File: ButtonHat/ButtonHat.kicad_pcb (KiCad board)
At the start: 2 copper layers, 65 x 56 mm, 40 parts, among them J0 RPI_GPIO, J1 1 2 3 4 5 6, J2 7 8 9 10 11 12, J3 4 17 27 22 5 6, J4 18 23 24 25 12 16, T1 1 2 3 4 5 6, T2 Ground, T3 7 8 9 10 11 12, U1 74AHC14, U2 74AHC14

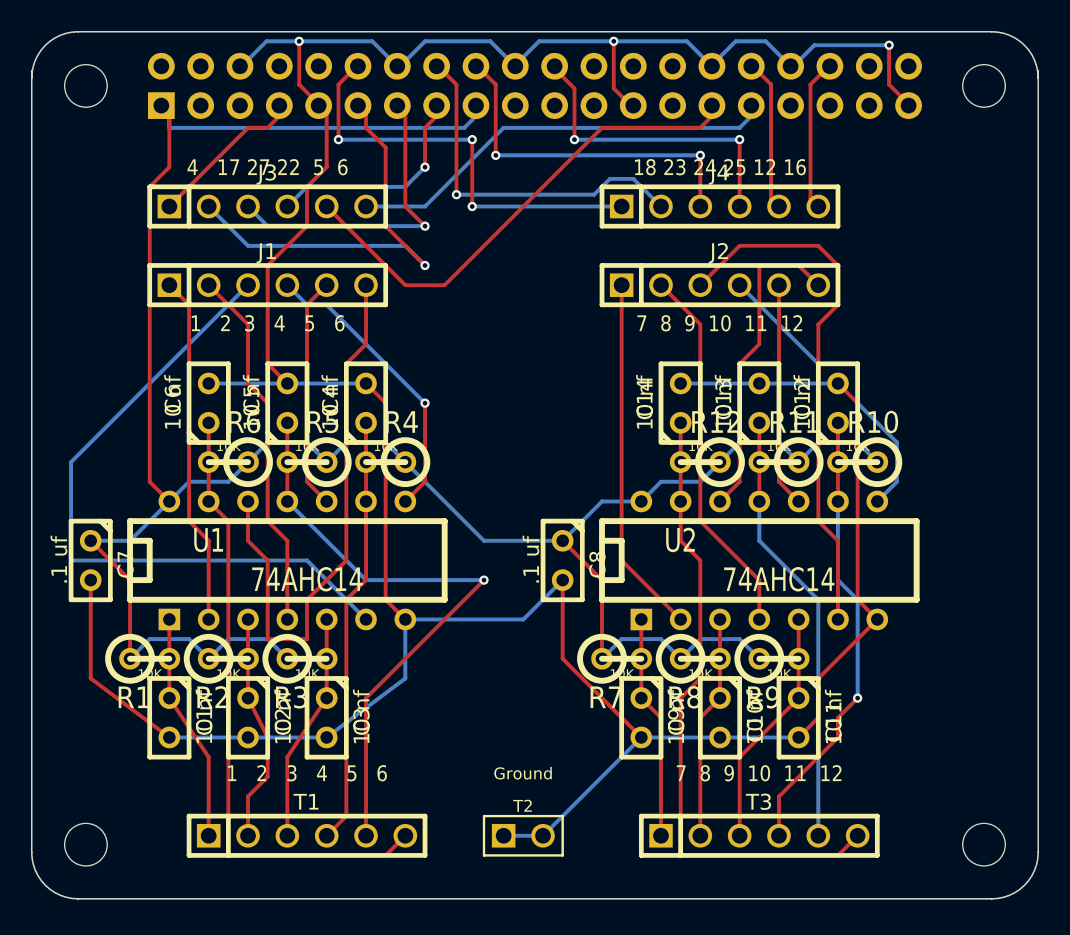
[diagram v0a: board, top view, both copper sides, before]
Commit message: Update GPIO Hats: make all 17 GPIO pins available on a socket header strip.
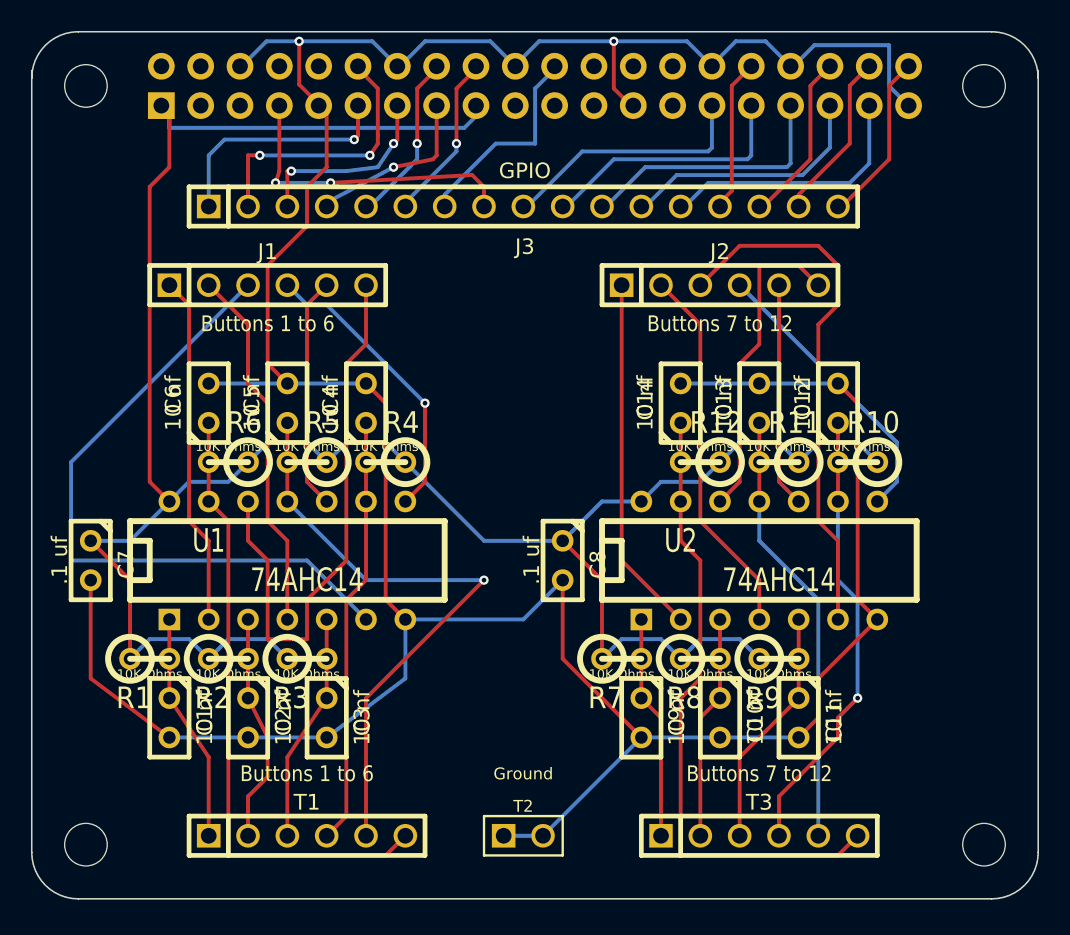
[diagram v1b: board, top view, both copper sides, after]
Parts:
- removed J4: 18 23 24 25 12 16, PIN_ARRAY-6X1
- J1: value 1 2 3 4 5 6 -> Buttons 1 to 6; footprint PIN_ARRAY-6X1 -> PIN_HEADER-6X1
- J2, T3: value 7 8 9 10 11 12 -> Buttons 7 to 12
- J3: value 4 17 27 22 5 6 -> GPIO; footprint PIN_ARRAY-6X1 -> PIN_HEADER_17x1
- R1, R10, R11, R12, R2, R3, R4, R5, R6, R7, R8, R9: value 10K -> 10K Ohms
- T1: value 1 2 3 4 5 6 -> Buttons 1 to 6
- moved J3 16.5 mm to (69.8, 43.2)
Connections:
- net N-0000013 renamed BCM22, wPi 3
- net N-0000014 renamed BCM27, wPi 2
- J0 pad 11: N-0000015 -> BCM17, wPi 0
- J0 pad 12: N-0000010 (its old number) -> BCM18, wPi 1
- J0 pad 16: N-0000022 -> BCM23, wPi 4
- J0 pad 18: N-000009 (its old number) -> BCM24, wPi 5
- J0 pad 22: N-000008 (its old number) -> BCM25, wPi 6
- J0 pad 29: N-0000012 -> BCM5, wPi 21
- J0 pad 31: N-0000011 -> BCM6, wPi 22
- J0 pad 32: N-000007 (its old number) -> BCM12, wPi 26
- J0 pad 33: (no net) -> BCM13, wPi 23
- J0 pad 35: (no net) -> BCM19, wPi 24
- J0 pad 36: N-0000024 -> BCM16, wPi 27
- J0 pad 37: (no net) -> BCM26, wPi 25
- J0 pad 38: (no net) -> BCM20, wPi 28
- J0 pad 40: (no net) -> BCM21, wPi 29
- J0 pad 7: N-0000016 -> BCM4, wPi 7
- J3 pad 1: N-0000016 -> BCM17, wPi 0
- J3 pad 2: N-0000015 -> BCM18, wPi 1
- J3 pad 5: N-0000012 -> BCM23, wPi 4
- J3 pad 6: N-0000011 -> BCM24, wPi 5
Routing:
- net N-0000012: track 32.8 -> 0.00 mm
- net N-0000011: track 28.6 -> 0.00 mm
- net N-0000010 (its old number): track 27.9 -> 0.00 mm, vias 3 -> 0
- net N-0000015: track 27.8 -> 0.00 mm, vias 1 -> 0
- net N-0000022: track 23.2 -> 0.00 mm, vias 1 -> 0
- net N-000009 (its old number): track 22.9 -> 0.00 mm, vias 2 -> 0
- net N-000008 (its old number): track 20.3 -> 0.00 mm, vias 2 -> 0
- net BCM4, wPi 7: track 0.00 -> 20.1 mm, vias 0 -> 2
- net BCM18, wPi 1: track 0.00 -> 17.6 mm, vias 0 -> 2
- net BCM26, wPi 25: track 0.00 -> 17.1 mm
- net BCM13, wPi 23: track 0.00 -> 17.1 mm
- net BCM6, wPi 22: track 0.00 -> 16.8 mm
- net BCM5, wPi 21: track 0.00 -> 16.5 mm
- net BCM19, wPi 24: track 0.00 -> 16.5 mm
- net BCM17, wPi 0: track 0.00 -> 15.4 mm, vias 0 -> 1
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
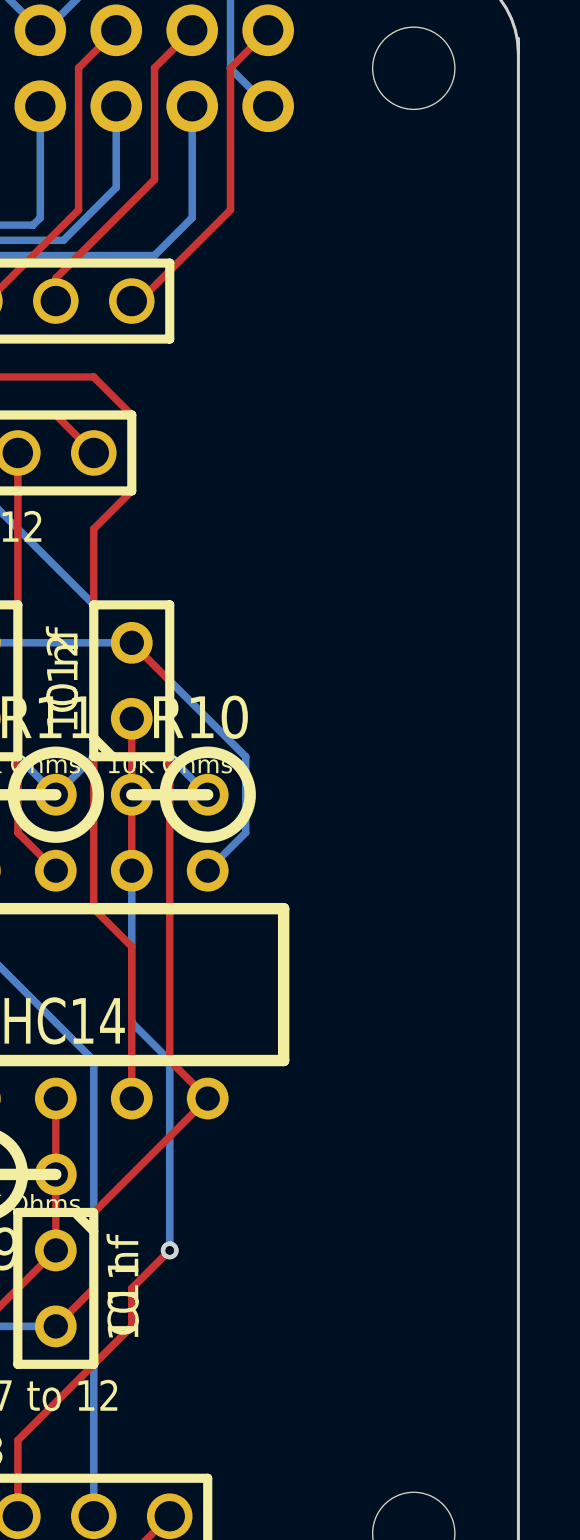
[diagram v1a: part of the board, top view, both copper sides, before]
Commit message: Add copyright notice to ButtonHat and LEDDriverHat.
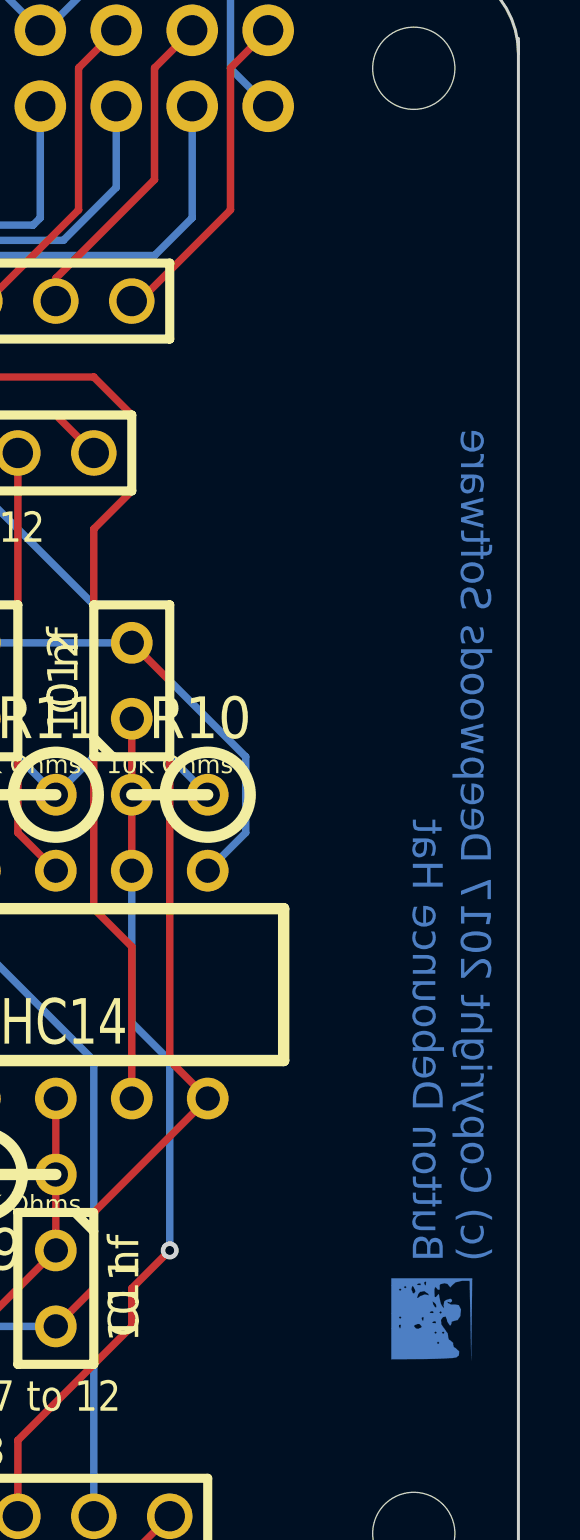
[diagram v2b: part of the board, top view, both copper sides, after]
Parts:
- added ?: , DWSLogoBCU, F.Cu at (100.2, 77.2)
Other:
- board text added: "(c) Copyright 2017 Deepwoods Software Button Debounce Hat"
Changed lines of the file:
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@@
     (area 29.28939 20.694 130.847429 101.769)
     (thickness 1.6)
-    (drawings 16)
+    (drawings 17)
     (tracks 345)
     (zones 0)
-    (modules 39)
+    (modules 40)
     (nets 44)
   )
@@
     )
   )
+  (module DWSLogoBCU (layer F.Cu)
+    (at 100.203 77.216 270)
+    (fp_text reference "" (at 0 0 270) (layer F.SilkS)
+      (effects (font (size 1.524 1.524) (thickness 0.15)))
+    )
+    (fp_text value "" (at 0 0 270) (layer F.SilkS)
+      (effects (font (size 1.524 1.524) (thickness 0.15)))
+    )
+    (fp_poly (pts (xy 1.397 -1.31826) (xy 0.0635 -1.29286) (xy -1.27 -1.26492) (xy -1.27 -1.01854)
+      (xy -1.2192 -0.79502) (xy -1.12268 -0.6858) (xy -1.04648 -0.61722) (xy -1.0795 -0.5969)
+      (xy -1.16586 -0.52324) (xy -1.18618 -0.42418) (xy -1.15824 -0.28956) (xy -1.12268 -0.26416)
+      (xy -0.9779 -0.26416) (xy -0.97028 -0.20828) (xy -1.016 -0.17018) (xy -1.06934 -0.11176)
+      (xy -0.9779 -0.0889) (xy -0.889 -0.0889) (xy -0.72898 -0.09906) (xy -0.7239 -0.1397)
+      (xy -0.762 -0.17018) (xy -0.83312 -0.23368) (xy -0.75184 -0.254) (xy -0.71882 -0.254)
+      (xy -0.51054 -0.30226) (xy -0.42418 -0.34798) (xy -0.34544 -0.41402) (xy -0.41148 -0.40386)
+      (xy -0.43688 -0.3937) (xy -0.58166 -0.41656) (xy -0.62738 -0.47752) (xy -0.6731 -0.62738)
+      (xy -0.635 -0.67564) (xy -0.58928 -0.67818) (xy -0.54102 -0.62484) (xy -0.5588 -0.57912)
+      (xy -0.56896 -0.5207) (xy -0.52832 -0.53848) (xy -0.47244 -0.65532) (xy -0.48006 -0.75184)
+      (xy -0.4572 -0.90424) (xy -0.30988 -0.9779) (xy -0.09144 -0.95758) (xy 0.04572 -0.86614)
+      (xy 0.0635 -0.77216) (xy 0.09652 -0.66802) (xy 0.15494 -0.65786) (xy 0.22352 -0.63246)
+      (xy 0.21336 -0.59436) (xy 0.0889 -0.51562) (xy 0.0381 -0.508) (xy -0.07366 -0.46482)
+      (xy -0.05588 -0.37338) (xy 0.04318 -0.30734) (xy 0.19304 -0.32512) (xy 0.3429 -0.42926)
+      (xy 0.49276 -0.53594) (xy 0.5969 -0.54864) (xy 0.69088 -0.56896) (xy 0.72898 -0.62992)
+      (xy 0.80772 -0.71882) (xy 0.85598 -0.71374) (xy 0.94488 -0.7366) (xy 0.98298 -0.8001)
+      (xy 1.08966 -0.91694) (xy 1.22428 -0.90678) (xy 1.2954 -0.81788) (xy 1.31318 -0.69088)
+      (xy 1.32842 -0.43434) (xy 1.34112 -0.08382) (xy 1.34874 0.32512) (xy 1.35636 1.35382)
+      (xy 0.84582 1.35382) (xy 0.84582 -0.21082) (xy 0.80518 -0.254) (xy 0.762 -0.21082)
+      (xy 0.80518 -0.17018) (xy 0.84582 -0.21082) (xy 0.84582 1.35382) (xy 0.508 1.35382)
+      (xy 0.508 -0.127) (xy 0.508 -0.381) (xy 0.46482 -0.42418) (xy 0.42418 -0.381)
+      (xy 0.46482 -0.33782) (xy 0.508 -0.381) (xy 0.508 -0.127) (xy 0.46482 -0.17018)
+      (xy 0.42418 -0.127) (xy 0.46482 -0.08382) (xy 0.508 -0.127) (xy 0.508 1.35382)
+      (xy 0.33782 1.35382) (xy 0.33782 0.46482) (xy 0.2921 0.35306) (xy 0.254 0.33782)
+      (xy 0.1778 0.4064) (xy 0.17018 0.46482) (xy 0.21336 0.57912) (xy 0.254 0.59182)
+      (xy 0.32766 0.52324) (xy 0.33782 0.46482) (xy 0.33782 1.35382) (xy 0.32258 1.35382)
+      (xy 0.32258 1.06934) (xy 0.30988 1.04394) (xy 0.20828 1.03378) (xy 0.19812 1.04394)
+      (xy 0.20828 1.09474) (xy 0.254 1.09982) (xy 0.32258 1.06934) (xy 0.32258 1.35382)
+      (xy 0.14986 1.35382) (xy 0.14986 -0.12954) (xy 0.1397 -0.14224) (xy 0.09144 -0.12954)
+      (xy 0.08382 -0.08382) (xy 0.1143 -0.01524) (xy 0.1397 -0.02794) (xy 0.14986 -0.12954)
+      (xy 0.14986 1.35382) (xy 0.06858 1.35382) (xy 0.06858 0.30734) (xy 0.05588 0.28194)
+      (xy -0.04572 0.27178) (xy -0.05588 0.28194) (xy -0.04572 0.33274) (xy 0 0.33782)
+      (xy 0.06858 0.30734) (xy 0.06858 1.35382) (xy 0 1.35382) (xy 0 1.05918)
+      (xy -0.04318 1.016) (xy -0.08382 1.05918) (xy -0.04318 1.09982) (xy 0 1.05918)
+      (xy 0 1.35382) (xy -0.17018 1.35382) (xy -0.17018 -0.29718) (xy -0.21082 -0.33782)
+      (xy -0.254 -0.29718) (xy -0.21082 -0.254) (xy -0.17018 -0.29718) (xy -0.17018 1.35382)
+      (xy -0.18796 1.35382) (xy -0.18796 -0.04572) (xy -0.19812 -0.05588) (xy -0.24892 -0.04572)
+      (xy -0.254 0) (xy -0.22352 0.06858) (xy -0.19812 0.05588) (xy -0.18796 -0.04572)
+      (xy -0.18796 1.35382) (xy -0.37846 1.35382) (xy -0.37846 -0.1524) (xy -0.4699 -0.14478)
+      (xy -0.53086 -0.09652) (xy -0.5842 -0.0254) (xy -0.50038 -0.04318) (xy -0.4826 -0.04826)
+      (xy -0.381 -0.1143) (xy -0.37846 -0.1524) (xy -0.37846 1.35382) (xy -0.6985 1.35382)
+      (xy -0.6985 0.4953) (xy -0.70612 0.44958) (xy -0.75946 0.38354) (xy -0.81534 0.23368)
+      (xy -0.8001 0.16002) (xy -0.78486 0.09652) (xy -0.83312 0.11938) (xy -0.92456 0.24638)
+      (xy -0.89916 0.39116) (xy -0.8255 0.45212) (xy -0.6985 0.4953) (xy -0.6985 1.35382)
+      (xy -0.84582 1.35382) (xy -0.84582 0.59436) (xy -0.90932 0.54864) (xy -0.97282 0.56134)
+      (xy -1.08458 0.6223) (xy -1.09982 0.64262) (xy -1.03124 0.6731) (xy -0.97282 0.67818)
+      (xy -0.86106 0.63246) (xy -0.84582 0.59436) (xy -0.84582 1.35382) (xy -0.93218 1.35382)
+      (xy -0.93218 1.05918) (xy -0.97282 1.016) (xy -1.016 1.05918) (xy -1.016 0.889)
+      (xy -1.05918 0.84582) (xy -1.09982 0.889) (xy -1.05918 0.93218) (xy -1.016 0.889)
+      (xy -1.016 1.05918) (xy -0.97282 1.09982) (xy -0.93218 1.05918) (xy -0.93218 1.35382)
+      (xy -1.11506 1.35382) (xy -1.11506 0.22352) (xy -1.1303 0.19812) (xy -1.22936 0.18796)
+      (xy -1.24206 0.19812) (xy -1.22936 0.24638) (xy -1.18618 0.254) (xy -1.11506 0.22352)
+      (xy -1.11506 1.35382) (xy -1.12014 1.35382) (xy -1.12014 0.37846) (xy -1.1303 0.36576)
+      (xy -1.17856 0.37846) (xy -1.18618 0.42418) (xy -1.1557 0.49276) (xy -1.1303 0.48006)
+      (xy -1.12014 0.37846) (xy -1.12014 1.35382) (xy -1.35382 1.35382) (xy -1.35382 0)
+      (xy -1.35382 -1.35382) (xy 0.02032 -1.33604) (xy 1.397 -1.31826) (xy 1.397 -1.31826)) (layer B.Cu) (width 0.00254))
+  )
+  (gr_text "(c) Copyright 2017 Deepwoods Software\nButton Debounce Hat" (at 100.838 75.311 270) (layer B.Cu)
+    (effects (font (size 1 1) (thickness 0.2)) (justify left mirror))
+  )
   (gr_arc (start 41.101 34.894) (end 38.101 34.894) (angle 90) (layer Edge.Cuts) (width 0.1))

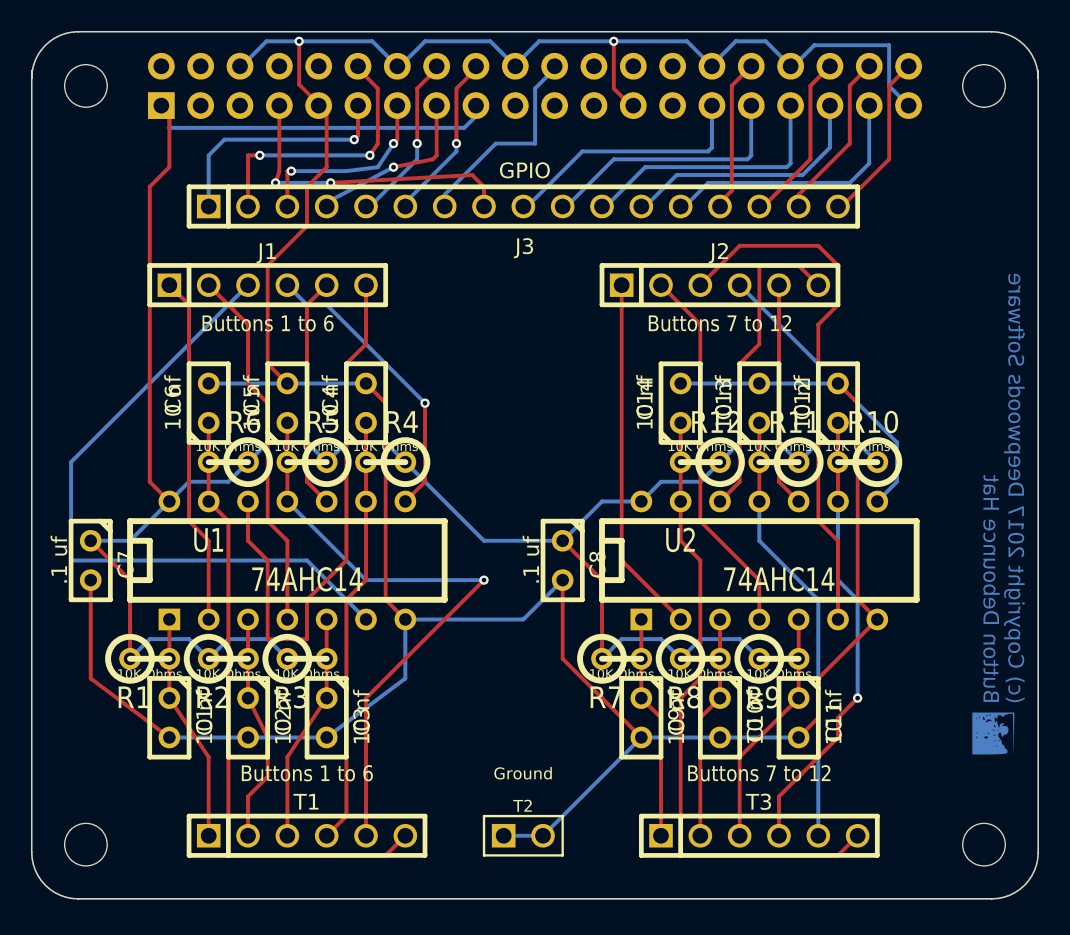
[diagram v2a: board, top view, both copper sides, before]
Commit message: Update 10nf caps to a stocked Mouser part.
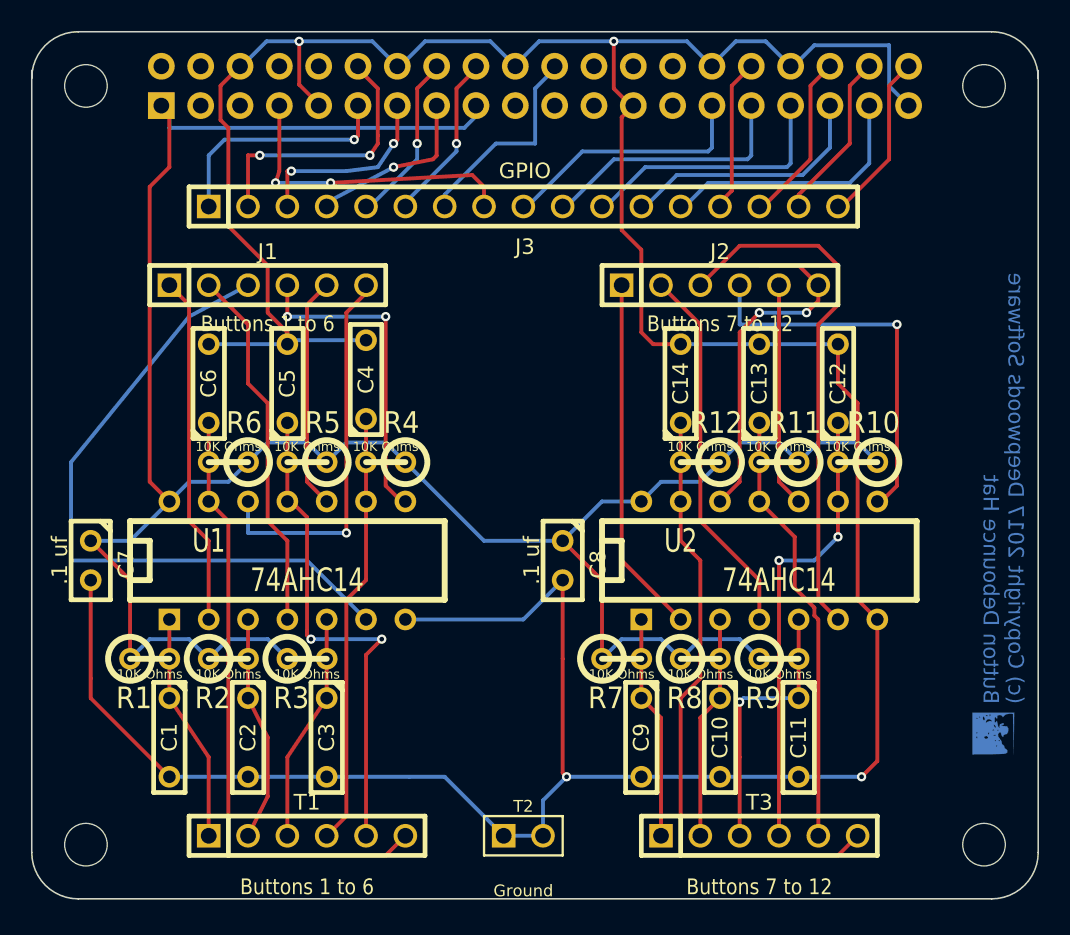
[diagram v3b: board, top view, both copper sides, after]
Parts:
- C1, C10, C11, C12, C13, C14, C2, C3, C4, C5, C6, C9: footprint C1 -> C2
- moved C4 1.52 mm to (59.7, 54.4)
- moved C12 1.27 mm to (90.2, 54.6)
- moved C13 1.27 mm to (85.1, 54.6)
- moved C14 1.27 mm to (80.0, 54.6)
- moved C5 1.27 mm to (54.6, 54.6)
- moved C6 1.27 mm to (49.5, 54.6)
- moved C1 1.27 mm to (47.0, 77.5)
- moved C10 1.27 mm to (82.5, 77.5)
- moved C11 1.27 mm to (87.6, 77.5)
- moved C2 1.27 mm to (52.1, 77.5)
- moved C3 1.27 mm to (57.1, 77.5)
- moved C9 1.27 mm to (77.5, 77.5)
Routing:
- net GND: track 223.1 -> 238.3 mm, vias 2 -> 4
- net N-0000028: track 36.4 -> 24.9 mm, vias 0 -> 1
- net N-0000033: track 39.6 -> 32.4 mm, vias 1 -> 2
- net N-000007: track 20.2 -> 24.8 mm, vias 0 -> 1
- net N-0000031: track 20.6 -> 22.7 mm, vias 0 -> 2
- net N-0000041: track 15.5 -> 17.6 mm, vias 0 -> 1
- net N-0000030: track 18.9 -> 21.0 mm, vias 1 -> 2
- net N-0000040: track 29.3 -> 29.6 mm, vias 1 -> 2
